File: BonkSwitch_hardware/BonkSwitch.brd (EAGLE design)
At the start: 100 x 62 mm, 96 parts, among them IC1 LMR16030SDDAR, IC2 LMR16006, IC3 FAN3227TMX, IC4 LMP8640, IC5 LMP8640, IC6 74LVC1G14DBV, Q1 SI2302, T1 IRF7493TRPBF, T2 IRF7493TRPBF, X1 XT60PW-M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

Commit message: More directory reorg
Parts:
- removed C12: 47uF 35V, rcl:C1210
- added C26: 120uF 35V, rcl:PANASONIC_E
- C11: value 47uF 35V -> 22uF 35V
- IC2: value LMR16006 -> LMR16006XDDC
- IC4, IC5: value LMP8640 -> LMP8640MK-T
- R1, R20: device rcl:R0805 -> rcl:R0603
- moved C11 27.4 mm to (76.8, 28.6), turned to 180 degrees
- moved LD4 0.63 mm to (76.8, 45.7)
- renumbered U$1 to LG1
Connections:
- net +24V: now also C26.+; no longer C12.1, LD4.A, LD5.A
- net +5V: now also LD4.A, LD5.A
- net GND: now also C26.-; no longer C12.2
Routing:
- net +5V: track 124.8 -> 177.2 mm, vias 6 -> 8
- net +24V: track 122.9 -> 108.5 mm
- net N$6: track 3.89 -> 3.35 mm
- net GND: vias 153 -> 171
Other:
- board text added: "It's Bonking Time"

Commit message: Tuning Schematic.
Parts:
- C11: value 22uF 35V -> 10uF 35V
- C14: value 1uF -> 10nF
- C2, C3, C7, C8: value 3.3uF 100V -> 2.2uF 100V
- Q1: value SI2302 -> SI2302CDS
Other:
- board text added: "Bonk Switch"
- board text removed: "Nelly Switch"

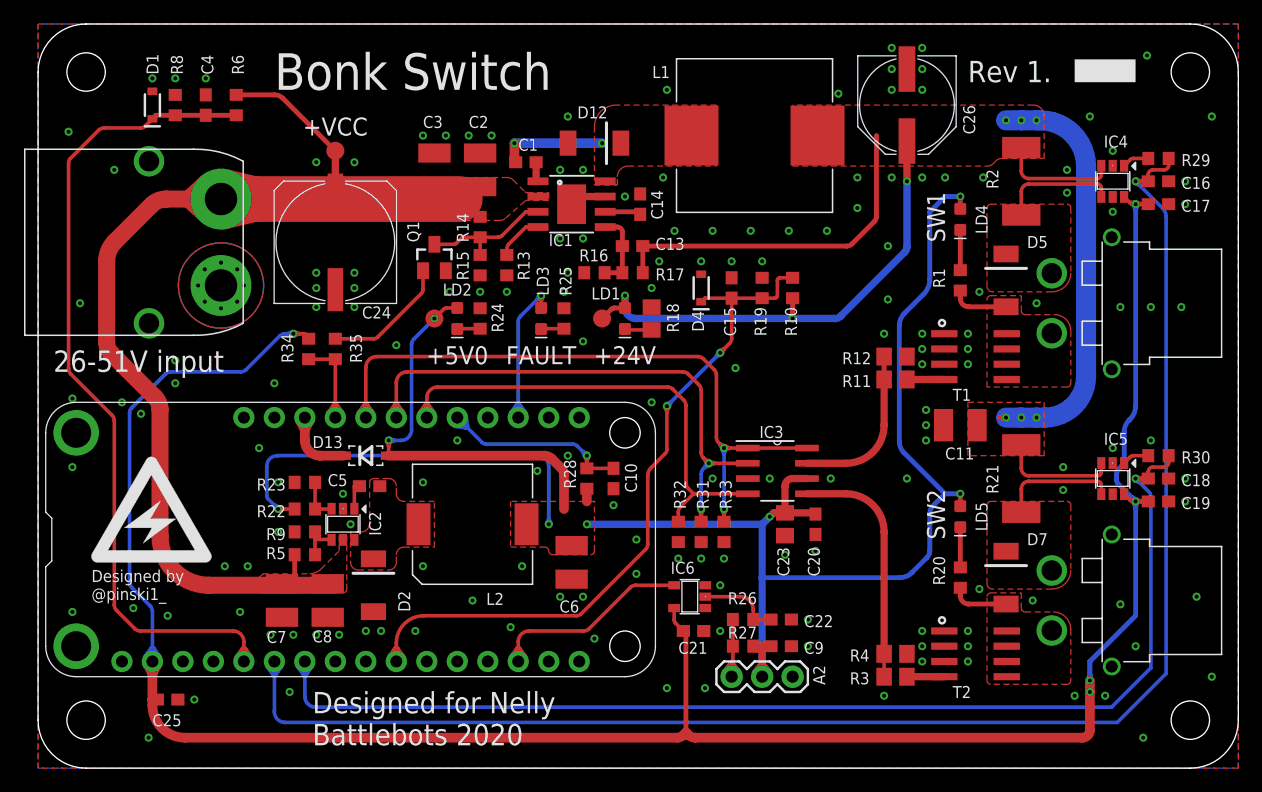
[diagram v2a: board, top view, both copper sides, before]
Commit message: Fixed SBUS bias resistor.
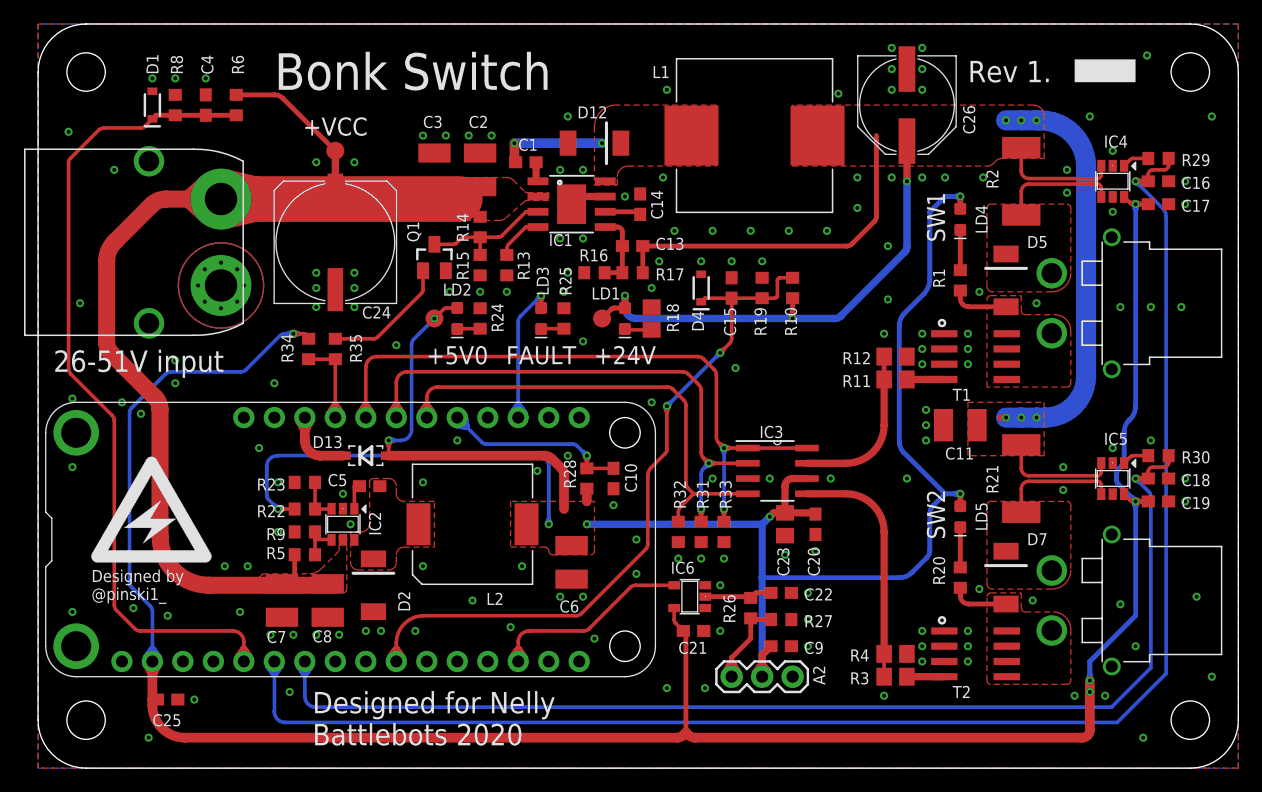
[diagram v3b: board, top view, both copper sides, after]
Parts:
- moved R27 3.88 mm to (61.9, 12.4)
- moved C22 2.22 mm to (61.9, 14.6)
- moved R26 1.14 mm to (59.4, 13.3), turned to 90 degrees
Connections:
- net +5V: no longer R27.1
- net GND: now also R27.1
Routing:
- net +3V3: track 206.5 -> 236.7 mm
- net +5V: track 177.2 -> 201.2 mm
- net EN_SW: track 63.1 -> 76.3 mm
- net SW1_EN: track 53.3 -> 64.4 mm
- net +24V: track 108.5 -> 115.4 mm
- net I_SW2_MON: track 101.0 -> 107.6 mm
- net I_SW1_MON: track 132.1 -> 138.8 mm
- net 5V_MON: track 20.7 -> 27.3 mm
- net FAULT: track 17.3 -> 23.9 mm
- net 24V_MON: track 66.4 -> 73.0 mm
- net GND: track 17.8 -> 23.0 mm, vias 171 -> 172
- net VCC_MON: track 70.5 -> 75.0 mm
- net SW2_EN: track 42.0 -> 46.4 mm
- net SBUS_IN: track 19.3 -> 23.7 mm
- net EN_PSU: track 9.88 -> 14.3 mm
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
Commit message: Moved +5V rail monitoring to A4
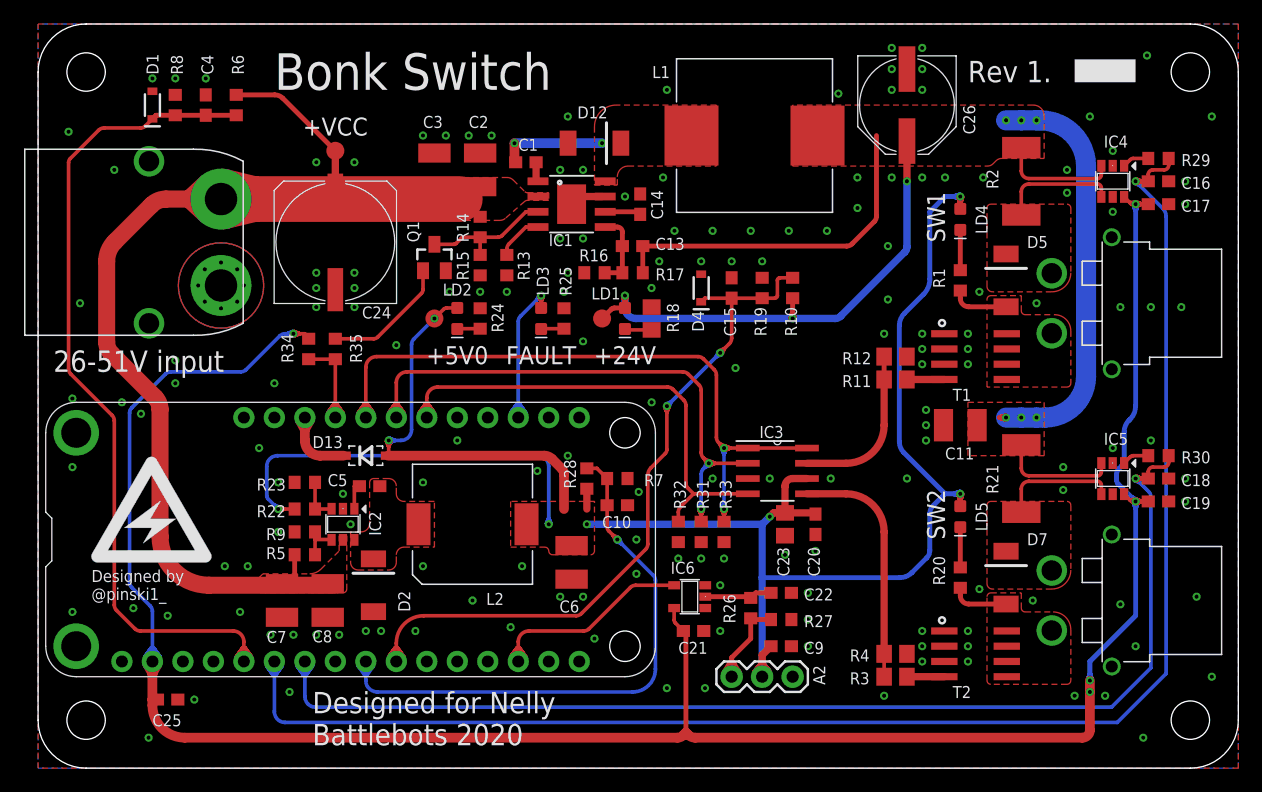
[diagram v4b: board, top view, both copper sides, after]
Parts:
- added R7: 33k, rcl:R0603
- R28: value 100k -> 47k
- moved C10 2.25 mm to (48.3, 21.9), turned to 0 degrees
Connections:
- removed net N$5: A1.9
- net 5V_MON: now also A1.9, R7.2; no longer A1.21
- net GND: now also R7.1
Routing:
- net +3V3: track 236.7 -> 266.5 mm
- net 5V_MON: track 27.3 -> 51.8 mm
- net +5V: track 201.2 -> 224.9 mm
- net EN_SW: track 76.3 -> 84.8 mm
- net SW1_EN: track 64.4 -> 71.7 mm
- net +24V: track 115.4 -> 121.2 mm
- net 24V_MON: track 73.0 -> 77.7 mm
- net FAULT: track 23.9 -> 28.7 mm
- net I_SW2_MON: track 107.6 -> 112.3 mm
- net I_SW1_MON: track 138.8 -> 143.5 mm
- net GND: track 23.0 -> 26.8 mm
- net SW2_EN: track 46.4 -> 50.0 mm
- net VCC_MON: track 75.0 -> 78.6 mm
- net EN_PSU: track 14.3 -> 17.9 mm
- net SBUS_IN: track 23.7 -> 27.3 mm

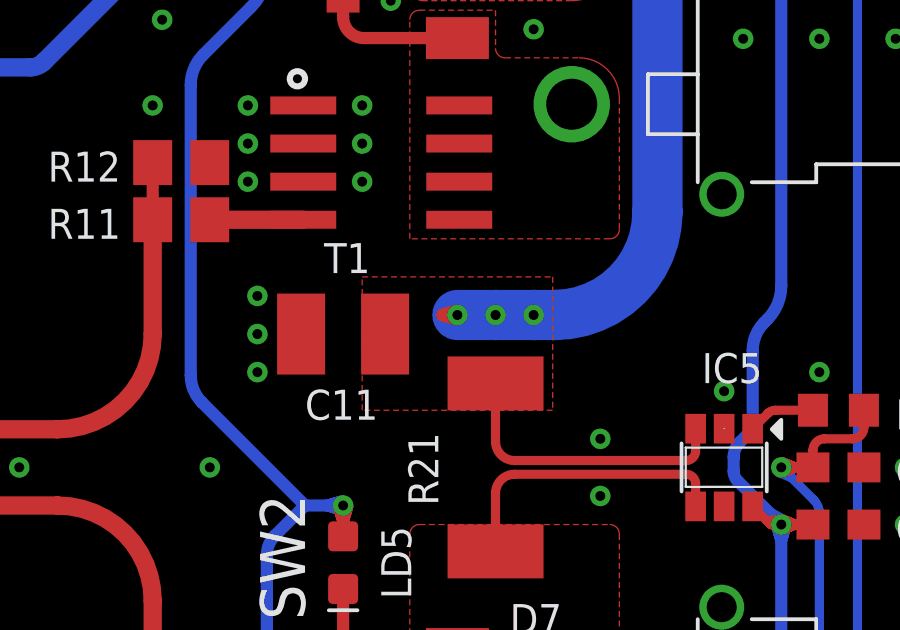
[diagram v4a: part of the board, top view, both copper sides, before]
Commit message: Updated schematic & BoM
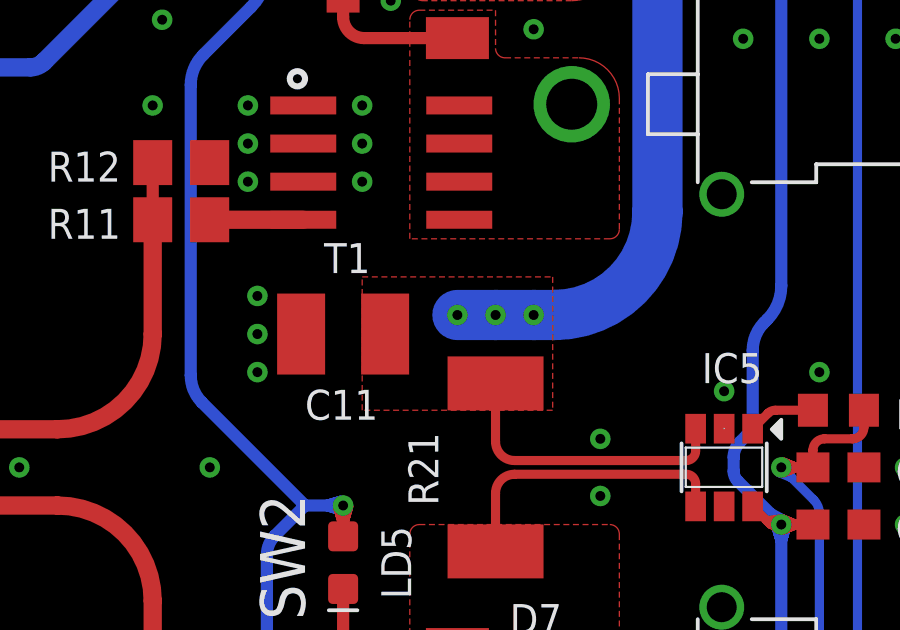
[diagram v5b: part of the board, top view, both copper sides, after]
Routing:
- net +24V: track 121.2 -> 115.0 mm
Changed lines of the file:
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@@
 <element name="X1" library="con-amass" package="XT60PW-M" value="XT60PW-M" x="15.24" y="43.815" smashed="yes" rot="R90">
 <attribute name="OC_FARNELL" value="unknown" x="15.24" y="43.815" size="1.778" layer="27" rot="R90" display="off"/>
-<attribute name="MF" value="Amass" x="15.24" y="43.815" size="1.778" layer="27" rot="R90" display="off"/>
+<attribute name="MF" value="" x="15.24" y="43.815" size="1.778" layer="27" rot="R90" display="off"/>
 <attribute name="MPN" value="" x="15.24" y="43.815" size="1.778" layer="27" rot="R90" display="off"/>
 </element>
 <element name="PCB1" library="dp_devices" package="DP10062_V1" value="PCB_DP_RECTANGLE-100X62" x="0" y="0" smashed="yes">
 <attribute name="OC_FARNELL" value="unknown" x="0" y="0" size="1.778" layer="27" display="off"/>
-<attribute name="MF" value="n/a" x="0" y="0" size="1.778" layer="27" display="off"/>
-<attribute name="MPN" value="n/a" x="0" y="0" size="1.778" layer="27" display="off"/>
+<attribute name="MF" value="" x="0" y="0" size="1.778" layer="27" display="off"/>
+<attribute name="MPN" value="" x="0" y="0" size="1.778" layer="27" display="off"/>
 </element>
 <element name="IC2" library="general" package="SOT23-6" value="LMR16006XDDC" x="25.4" y="20.32" smashed="yes" rot="R180">
@@
 <element name="X2" library="con-amass" package="XT30PW-F" value="XT30PW-F" x="84.455" y="38.735" smashed="yes" rot="R270">
 <attribute name="OC_FARNELL" value="unknown" x="84.455" y="38.735" size="1.778" layer="27" rot="R270" display="off"/>
-<attribute name="MF" value="Amass" x="84.455" y="38.735" size="1.778" layer="27" rot="R270" display="off"/>
+<attribute name="MF" value="" x="84.455" y="38.735" size="1.778" layer="27" rot="R270" display="off"/>
 <attribute name="MPN" value="" x="84.455" y="38.735" size="1.778" layer="27" rot="R270" display="off"/>
 </element>
 <element name="X3" library="con-amass" package="XT30PW-F" value="XT30PW-F" x="84.455" y="13.97" smashed="yes" rot="R270">
 <attribute name="OC_FARNELL" value="unknown" x="84.455" y="13.97" size="1.778" layer="27" rot="R270" display="off"/>
-<attribute name="MF" value="Amass" x="84.455" y="13.97" size="1.778" layer="27" rot="R270" display="off"/>
+<attribute name="MF" value="" x="84.455" y="13.97" size="1.778" layer="27" rot="R270" display="off"/>
 <attribute name="MPN" value="" x="84.455" y="13.97" size="1.778" layer="27" rot="R270" display="off"/>
 </element>
@@
 <element name="A1" library="ThingySticks" package="FEATHERWING_DIM" value="FEATHERWING_NODIM" x="0.635" y="7.62" smashed="yes">
 <attribute name="OC_FARNELL" value="unknown" x="0.635" y="7.62" size="1.778" layer="27" display="off"/>
-<attribute name="MF" value="n/a" x="0.635" y="7.62" size="1.778" layer="27" display="off"/>
-<attribute name="MPN" value="n/a" x="0.635" y="7.62" size="1.778" layer="27" display="off"/>
+<attribute name="MF" value="" x="0.635" y="7.62" size="1.778" layer="27" display="off"/>
+<attribute name="MPN" value="" x="0.635" y="7.62" size="1.778" layer="27" display="off"/>
 </element>
 <element name="C20" library="rcl" package="C0603" value="100nF" x="64.77" y="20.32" smashed="yes" rot="R270">
@@
 <attribute name="VALUE" x="64.135" y="9.652" size="1" layer="27" font="vector" ratio="11" rot="R180"/>
 <attribute name="OC_FARNELL" value="unknown" x="62.865" y="7.62" size="1.778" layer="27" rot="R90" display="off"/>
-<attribute name="MF" value="FrSky" x="62.865" y="7.62" size="1.778" layer="27" rot="R90" display="off"/>
-<attribute name="MPN" value="XM" x="62.865" y="7.62" size="1.778" layer="27" rot="R90" display="off"/>
+<attribute name="MF" value="" x="62.865" y="7.62" size="1.778" layer="27" rot="R90" display="off"/>
+<attribute name="MPN" value="" x="62.865" y="7.62" size="1.778" layer="27" rot="R90" display="off"/>
 </element>
 <element name="LG1" library="general" package="LOGO_10X10" value="" x="4.445" y="17.145"/>
@@
 <contactref element="C26" pad="+"/>
 <contactref element="C11" pad="1"/>
-<wire x1="80.1497" y1="29.21" x2="80.645" y2="29.21" width="0.4064" layer="1"/>
 <wire x1="48.895" y1="38.8747" x2="49.029025" y2="39.33059375" width="0.4064" layer="1"/>
 <wire x1="48.895" y1="38.8747" x2="49.029028125" y2="39.33059375" width="0.4064" layer="1"/>
@@
 <wire x1="62.999028125" y1="37.504403125" x2="62.999028125" y2="37.5044" width="0.4064" layer="1"/>
 <wire x1="62.865" y1="37.465" x2="62.999028125" y2="37.5044" width="0.4064" layer="1"/>
-<wire x1="80.149696875" y1="29.21" x2="80.1497" y2="29.21" width="0.4064" layer="1"/>
-<wire x1="80.1497" y1="29.21" x2="80.60559375" y2="29.344025" width="0.4064" layer="1"/>
-<wire x1="80.605596875" y1="29.075971875" x2="80.605596875" y2="29.07596875" width="0.4064" layer="1"/>
-<wire x1="80.60559375" y1="29.344025" x2="80.605596875" y2="29.344025" width="0.4064" layer="1"/>
-<wire x1="80.645" y1="29.21" x2="80.605596875" y2="29.344025" width="0.4064" layer="1"/>
-<wire x1="80.1497" y1="29.21" x2="80.60559375" y2="29.075971875" width="0.4064" layer="1"/>
-<wire x1="80.60559375" y1="29.075971875" x2="80.605596875" y2="29.075971875" width="0.4064" layer="1"/>
-<wire x1="80.645" y1="29.21" x2="80.605596875" y2="29.075971875" width="0.4064" layer="1"/>
-<wire x1="80.1497" y1="29.21" x2="80.60559375" y2="29.344028125" width="0.4064" layer="1"/>
-<wire x1="80.60559375" y1="29.344028125" x2="80.605596875" y2="29.344028125" width="0.4064" layer="1"/>
-<wire x1="80.645" y1="29.21" x2="80.605596875" y2="29.344028125" width="0.4064" layer="1"/>
 <wire x1="48.895" y1="38.874696875" x2="49.029025" y2="39.33059375" width="0.4064" layer="1"/>
 <wire x1="48.894996875" y1="38.874696875" x2="48.894996875" y2="38.8747" width="0.4064" layer="1"/>
@@
 <wire x1="62.864996875" y1="37.960303125" x2="62.999025" y2="37.504403125" width="0.4064" layer="1"/>
 <wire x1="62.865" y1="37.465" x2="62.999025" y2="37.504403125" width="0.4064" layer="1"/>
-<wire x1="80.149696875" y1="29.21" x2="80.60559375" y2="29.344025" width="0.4064" layer="1"/>
-<wire x1="80.60559375" y1="29.075971875" x2="80.60559375" y2="29.07596875" width="0.4064" layer="1"/>
-<wire x1="80.149696875" y1="29.209996875" x2="80.1497" y2="29.209996875" width="0.4064" layer="1"/>
-<wire x1="80.1497" y1="29.209996875" x2="80.60559375" y2="29.07596875" width="0.4064" layer="1"/>
-<wire x1="80.60559375" y1="29.07596875" x2="80.605596875" y2="29.07596875" width="0.4064" layer="1"/>
-<wire x1="80.645" y1="29.21" x2="80.605596875" y2="29.07596875" width="0.4064" layer="1"/>
-<wire x1="80.1497" y1="29.209996875" x2="80.60559375" y2="29.344025" width="0.4064" layer="1"/>
-<wire x1="80.149696875" y1="29.21" x2="80.60559375" y2="29.075971875" width="0.4064" layer="1"/>
-<wire x1="80.645" y1="29.21" x2="80.60559375" y2="29.075971875" width="0.4064" layer="1"/>
-<wire x1="80.149696875" y1="29.21" x2="80.60559375" y2="29.344028125" width="0.4064" layer="1"/>
-<wire x1="80.60559375" y1="29.344025" x2="80.60559375" y2="29.344028125" width="0.4064" layer="1"/>
-<wire x1="80.149696875" y1="29.209996875" x2="80.60559375" y2="29.07596875" width="0.4064" layer="1"/>
-<wire x1="80.645" y1="29.21" x2="80.60559375" y2="29.07596875" width="0.4064" layer="1"/>
-<wire x1="80.149696875" y1="29.209996875" x2="80.60559375" y2="29.344025" width="0.4064" layer="1"/>
-<wire x1="80.645" y1="29.21" x2="80.60559375" y2="29.344025" width="0.4064" layer="1"/>
 </signal>
 <signal name="RT_24V">
